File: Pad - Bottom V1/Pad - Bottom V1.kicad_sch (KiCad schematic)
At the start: 1 part, among them J1 B2B-XH-A

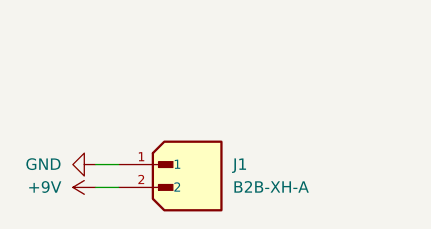
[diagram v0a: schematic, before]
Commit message: Finally fixed the issues with folder and file naming.
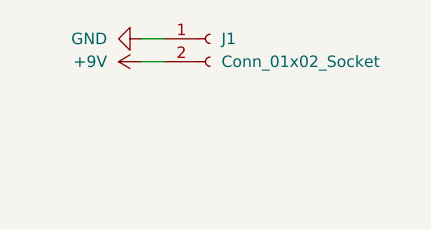
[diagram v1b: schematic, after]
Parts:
- removed J1: B2B-XH-A, B2B-XH-A:B2B-XH-A, symbol B2B-XH-A:B2B-XH-A
- added J1: Conn_01x02_Socket, Connector_AMASS:AMASS_XT30U-M_1x02_P5.0mm_Vertical, symbol Connector:Conn_01x02_Socket
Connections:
- net +9V: now also J1.2 (Pin_2)
- net GND: now also J1.1 (Pin_1)
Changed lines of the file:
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@@
 	(wire
 		(pts
-			(xy 146.05 100.33) (xy 148.59 100.33)
+			(xy 151.13 86.36) (xy 153.67 86.36)
 		)
 		(stroke
@@
 	(wire
 		(pts
-			(xy 146.05 102.87) (xy 148.59 102.87)
+			(xy 151.13 88.9) (xy 153.67 88.9)
 		)
 		(stroke
@@
 	)
 	(symbol
+		(lib_id "Connector:Conn_01x02_Socket")
+		(at 158.75 86.36 0)
+		(unit 1)
+		(exclude_from_sim no)
+		(in_bom yes)
+		(on_board yes)
+		(dnp no)
+		(fields_autoplaced yes)
+		(property "Reference" "J1"
+			(at 160.02 86.3599 0)
+			(effects
+				(font
+					(size 1.27 1.27)
+				)
+				(justify left)
+			)
+		)
+		(property "Value" "Conn_01x02_Socket"
+			(at 160.02 88.8999 0)
+			(effects
+				(font
+					(size 1.27 1.27)
+				)
+				(justify left)
+			)
+		)
+		(property "Footprint" "Connector_AMASS:AMASS_XT30U-M_1x02_P5.0mm_Vertical"
+			(at 158.75 86.36 0)
+			(effects
+				(font
+					(size 1.27 1.27)
+				)
+				(hide yes)
+			)
+		)
+		(property "Datasheet" "https://www.tme.com/Document/7d9d972ae3468777f69ec2ee99897652/XT30U-M.pdf"
+			(at 158.75 86.36 0)
+			(effects
+				(font
+					(size 1.27 1.27)
+				)
+				(hide yes)
+			)
+		)
+		(property "Description" "2 PIN XT30 Male"
+			(at 158.75 86.36 0)
+			(effects
+				(font
+					(size 1.27 1.27)
+				)
+				(hide yes)
+			)
+		)
+		(property "Mfr." "TME"
+			(at 158.75 86.36 0)
+			(effects
+				(font
+					(size 1.27 1.27)
+				)
+				(hide yes)
+			)
+		)
+		(property "Part #" "XT30U-M"
+			(at 158.75 86.36 0)
+			(effects
+				(font
+					(size 1.27 1.27)
+				)
+				(hide yes)
+			)
+		)
+		(property "Order Link" "https://www.tme.com/us/en-us/details/xt30u-m/dc-power-connectors/amass/"
+			(at 158.75 86.36 0)
+			(effects
+				(font
+					(size 1.27 1.27)
+				)
+				(hide yes)
+			)
+		)
+		(property "Price" "$0.626"
+			(at 158.75 86.36 0)
+			(effects
+				(font
+					(size 1.27 1.27)
+				)
+				(hide yes)
+			)
+		)
+		(pin "1"
+		)
+		(pin "2"
+		)
+		(instances
+			(project ""
+				(path "/3290a135-58b8-4768-b0c2-c03f3bc7cf69"
+					(reference "J1")
+					(unit 1)
+				)
+			)
+		)
+	)
+	(symbol
+		(lib_id "power:+9V")
+		(at 151.13 88.9 90)
+		(unit 1)
+		(exclude_from_sim no)
+		(in_bom yes)
+		(on_board yes)
+		(dnp no)
+		(fields_autoplaced yes)
+		(property "Reference" "#PWR02"
+			(at 154.94 88.9 0)
+			(effects
+				(font
+					(size 1.27 1.27)
+				)
+				(hide yes)
+			)
+		)
+		(property "Value" "+9V"
+			(at 147.32 88.8999 90)
+			(effects
+				(font
+					(size 1.27 1.27)
+				)
+				(justify left)
+			)
+		)
+		(property "Footprint" ""
+			(at 151.13 88.9 0)
+			(effects
+				(font
+					(size 1.27 1.27)
+				)
+				(hide yes)
+			)
+		)
+		(property "Datasheet" ""
+			(at 151.13 88.9 0)
+			(effects
+				(font
+					(size 1.27 1.27)
+				)
+				(hide yes)
+			)
+		)
+		(property "Description" "Power symbol creates a global label with name \"+9V\""
+			(at 151.13 88.9 0)
+			(effects
+				(font
+					(size 1.27 1.27)
+				)
+				(hide yes)
+			)
+		)
+		(pin "1"
+		)
+		(instances
+			(project ""
+				(path "/3290a135-58b8-4768-b0c2-c03f3bc7cf69"
+					(reference "#PWR02")
+					(unit 1)
+				)
+			)
+		)
+	)
+	(symbol
 		(lib_id "power:GND")
-		(at 146.05 100.33 270)
+		(at 151.13 86.36 270)
 		(unit 1)
 		(exclude_from_sim no)
@@
 		(fields_autoplaced yes)
 		(property "Reference" "#PWR01"
-			(at 139.7 100.33 0)
+			(at 144.78 86.36 0)
 			(effects
 				(font
@@
 		)
 		(property "Value" "GND"
-			(at 142.24 100.3299 90)
+			(at 147.32 86.3599 90)
 			(effects
 				(font
@@
 		)
 		(property "Footprint" ""
-			(at 146.05 100.33 0)
+			(at 151.13 86.36 0)
 			(effects
 				(font
@@
 		)
 		(property "Datasheet" ""
-			(at 146.05 100.33 0)
+			(at 151.13 86.36 0)
 			(effects
 				(font
@@
 		)
 		(property "Description" "Power symbol creates a global label with name \"GND\" , ground"
-			(at 146.05 100.33 0)
+			(at 151.13 86.36 0)
 			(effects
 				(font
@@
 		(instances
 			(project ""
-				(path "/f2fb824b-0c7c-4faa-907c-a8c85c24ff79"
+				(path "/3290a135-58b8-4768-b0c2-c03f3bc7cf69"
 					(reference "#PWR01")
 					(unit 1)
 				)
-			)
-		)
-	)
-	(symbol
-		(lib_id "power:+9V")
-		(at 146.05 102.87 90)
-		(unit 1)
-		(exclude_from_sim no)
-		(in_bom yes)
-		(on_board yes)
-		(dnp no)
-		(fields_autoplaced yes)
-		(property "Reference" "#PWR02"
-			(at 149.86 102.87 0)
-			(effects
-				(font
-					(size 1.27 1.27)
-				)
-				(hide yes)
-			)
-		)
-		(property "Value" "+9V"
-			(at 142.24 102.8699 90)
-			(effects
-				(font
-					(size 1.27 1.27)
-				)
-				(justify left)
-			)
-		)
-		(property "Footprint" ""
-			(at 146.05 102.87 0)
-			(effects
-				(font
-					(size 1.27 1.27)
-				)
-				(hide yes)
-			)
-		)
-		(property "Datasheet" ""
-			(at 146.05 102.87 0)
-			(effects
-				(font
-					(size 1.27 1.27)
-				)
-				(hide yes)
-			)
-		)
-		(property "Description" "Power symbol creates a global label with name \"+9V\""
-			(at 146.05 102.87 0)
-			(effects
-				(font
-					(size 1.27 1.27)
-				)
-				(hide yes)
-			)
-		)
-		(pin "1"
-		)
-		(instances
-			(project ""
-				(path "/f2fb824b-0c7c-4faa-907c-a8c85c24ff79"
-					(reference "#PWR02")
-					(unit 1)
-				)
-			)
-		)
-	)
-	(symbol
-		(lib_id "B2B-XH-A:B2B-XH-A")
-		(at 156.21 102.87 0)
-		(unit 1)
-		(exclude_from_sim no)
-		(in_bom yes)
-		(on_board yes)
-		(dnp no)
-		(fields_autoplaced yes)
-		(property "Reference" "J1"
-			(at 161.29 100.3299 0)
-			(effects
-				(font
-					(size 1.27 1.27)
-				)
-				(justify left)
-			)
-		)
-		(property "Value" "B2B-XH-A"
-			(at 161.29 102.8699 0)
-			(effects
-				(font
-					(size 1.27 1.27)
-				)
-				(justify left)
-			)
-		)
-		(property "Footprint" "B2B-XH-A:B2B-XH-A"
-			(at 156.21 102.87 0)
-			(effects
-				(font
-					(size 1.27 1.27)
-				)
-				(justify bottom)
-				(hide yes)
-			)
-		)
-		(property "Datasheet" ""
-			(at 156.21 102.87 0)
-			(effects
-				(font
-					(size 1.27 1.27)
-				)
-				(hide yes)
-			)
-		)
-		(property "Description" ""
-			(at 156.21 102.87 0)
-			(effects
-				(font
-					(size 1.27 1.27)
-				)
-				(hide yes)
-			)
-		)
-		(property "PARTREV" "N/A"
-			(at 156.21 102.87 0)
-			(effects
-				(font
-					(size 1.27 1.27)
-				)
-				(justify bottom)
-				(hide yes)
-			)
-		)
-		(property "STANDARD" "Manufacturer Recommendations"
-			(at 156.21 102.87 0)
-			(effects
-				(font
-					(size 1.27 1.27)
-				)
-				(justify bottom)
-				(hide yes)
-			)
-		)
-		(property "MAXIMUM_PACKAGE_HEIGHT" "7 mm"
-			(at 156.21 102.87 0)
-			(effects
-				(font
-					(size 1.27 1.27)
-				)
-				(justify bottom)
-				(hide yes)
-			)
-		)
-		(property "MANUFACTURER" "JST Sales America Inc."
-			(at 156.21 102.87 0)
-			(effects
-				(font
-					(size 1.27 1.27)
-				)
-				(justify bottom)
-				(hide yes)
-			)
-		)
-		(pin "1"
-		)
-		(pin "2"
-		)
-		(instances
-			(project ""
-				(path "/f2fb824b-0c7c-4faa-907c-a8c85c24ff79"
-					(reference "J1")
-					(unit 1)
-				)
